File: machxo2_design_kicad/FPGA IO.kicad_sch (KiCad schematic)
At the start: 3 parts, among them J2 Conn_01x12_Pin, J3 Conn_01x12_Pin, U1 LCMX02-256HC-4SG32C

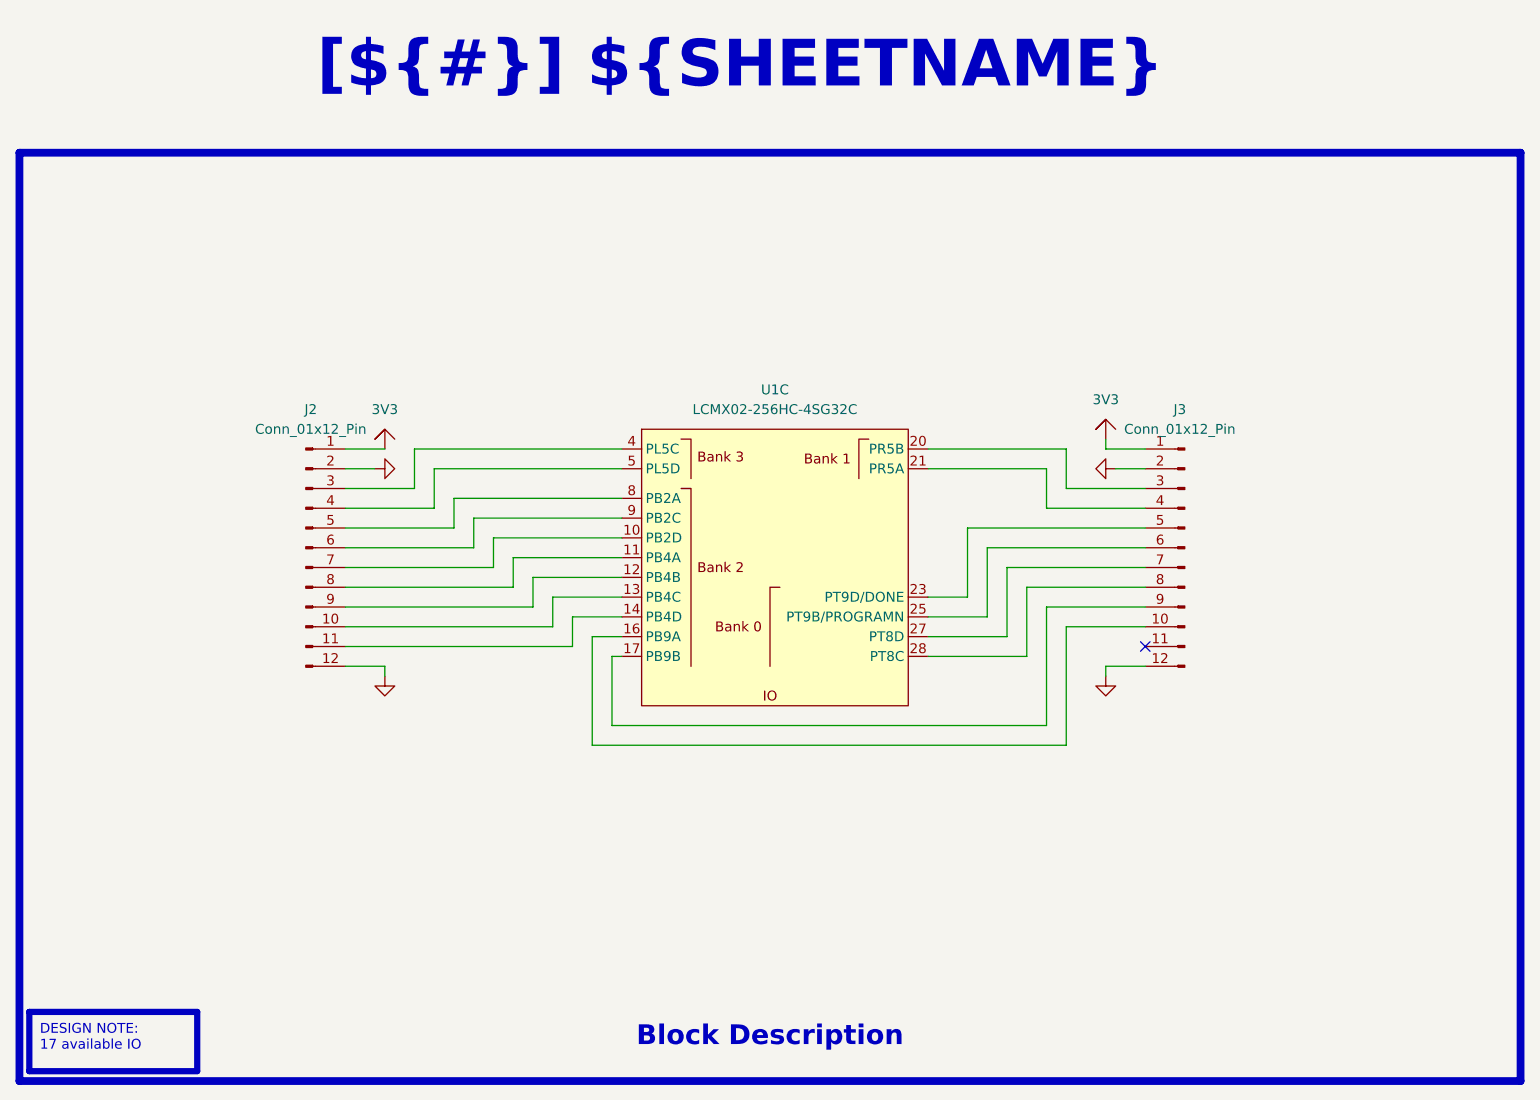
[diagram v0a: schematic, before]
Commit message: Prelimary schematic done. Need to create BOM and review.
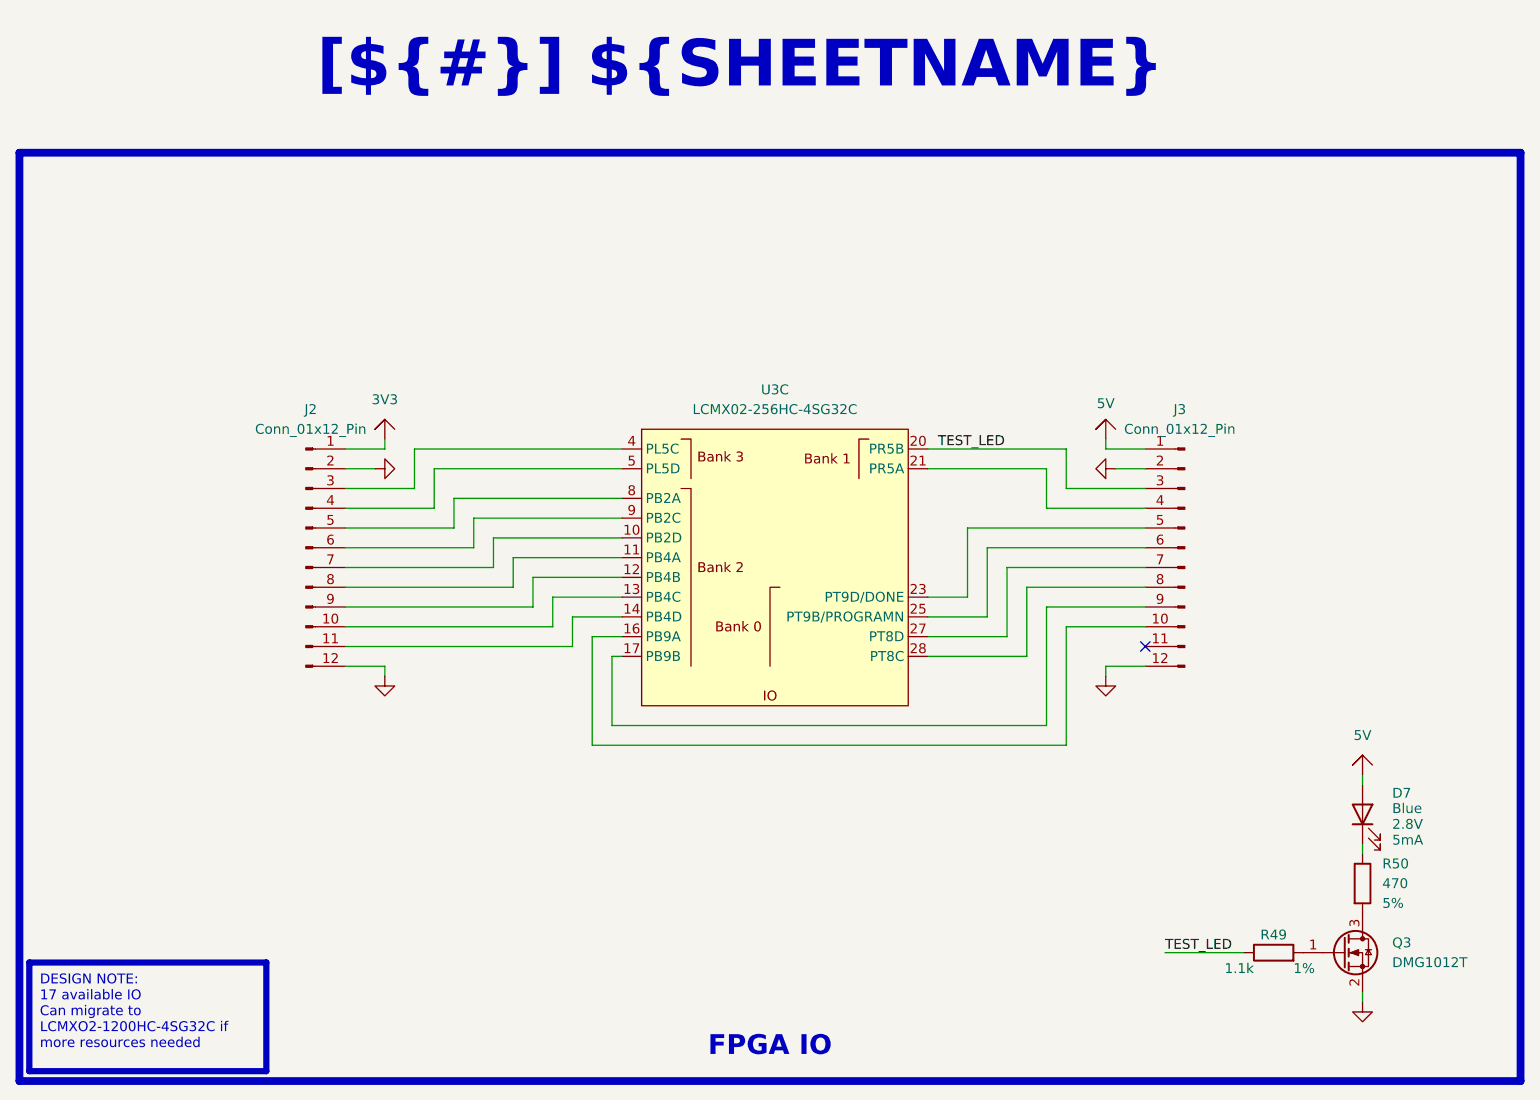
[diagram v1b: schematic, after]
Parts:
- added D7: Blue, 0_LED:LED_0603_1608Metric, symbol Device:LED
- added Q3: DMG1012T, 0_FET:SOT-523, symbol Transistor_FET:Q_NMOS_GSD
- added R49: 1.1k, symbol Device:R
- added R50: 470, symbol Device:R
- U3: renamed from U1; footprint (none) -> 0_FPGA:kicad_QFN-32-1EP_5x5mm_P0.5mm_EP3.2x3.2mm
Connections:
- net 3V3: no longer J3.1 (Pin_1)
- net GND: now also Q3.2 (S)
- net TEST_LED: now reaches J3.3 (Pin_3), U3.20 (PR5B)
- net TEST_LED: now also R49.1
- new net: D7.1 (K), R50.1
- new net: Q3.1 (G), R49.2
- new net: Q3.3 (D), R50.2
- new net 5V: D7.2 (A), J3.1 (Pin_1)
